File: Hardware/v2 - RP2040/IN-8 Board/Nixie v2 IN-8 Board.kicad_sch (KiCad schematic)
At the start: 31 parts, among them J1 Conn_01x10_Pin, J2 Conn_01x10_Pin, J3 Conn_01x10_Pin, Q1 MMBTA42, Q2 PZTA92, U1 NCH8200HV, U2 VEML7700, U3 К155ИД1, U4 К155ИД1, U5 К155ИД1, U6 К155ИД1

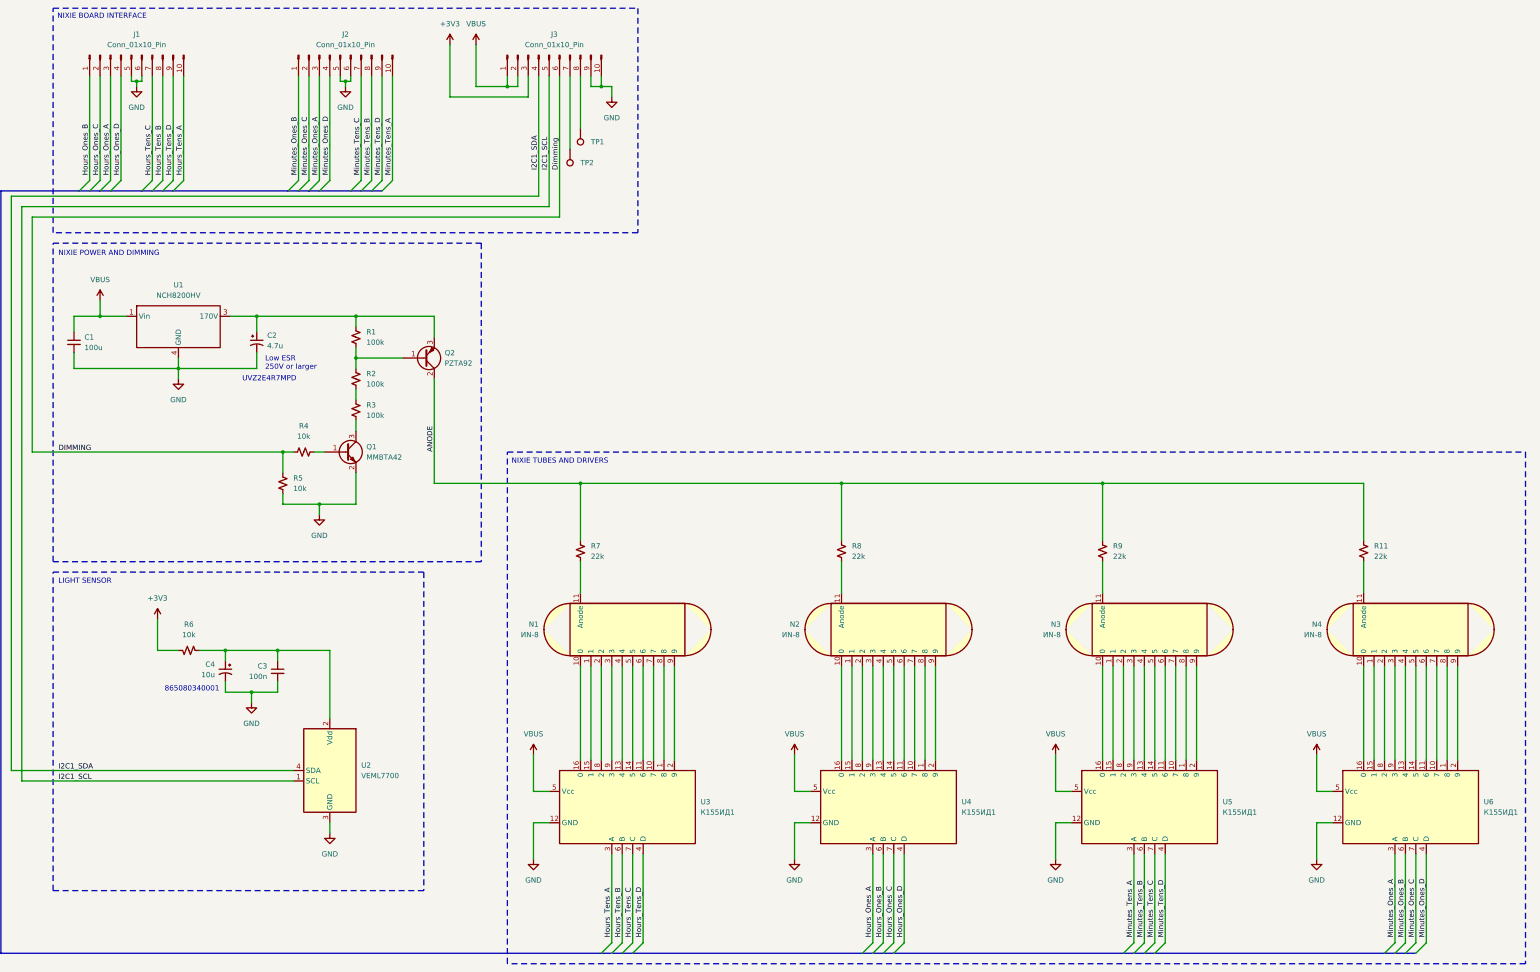
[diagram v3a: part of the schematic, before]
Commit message: started nixie layout, added bleed resistor to HV cap
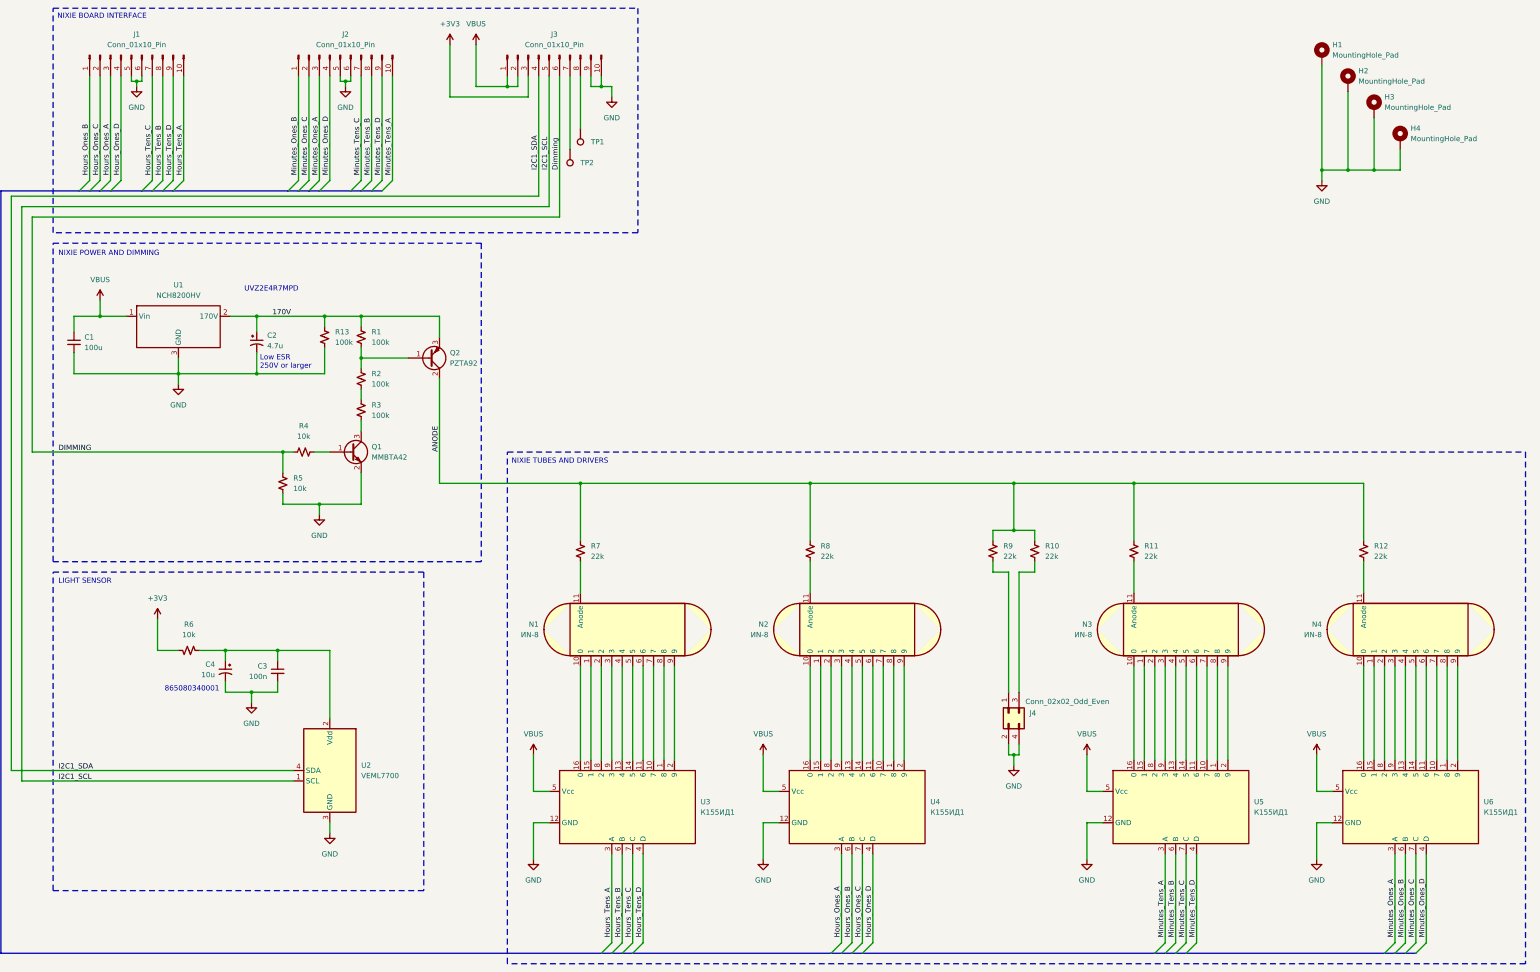
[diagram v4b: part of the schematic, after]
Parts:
- added H1, H2, H3, H4: MountingHole_Pad, MountingHole:MountingHole_3.2mm_M3_Pad_Via, symbol Mechanical:MountingHole_Pad
- added J4: Conn_02x02_Odd_Even, Connector_PinSocket_2.54mm:PinSocket_2x02_P2.54mm_Vertical, symbol Connector_Generic:Conn_02x02_Odd_Even
- added R10, R9: 22k, Resistor_SMD:R_0805_2012Metric, symbol Device:R_Small_US
- added R13: 100k, Resistor_SMD:R_0805_2012Metric, symbol Device:R_Small_US
- J1, J2, J3: footprint Connector_PinHeader_2.54mm:PinHeader_2x05_P2.54mm_Horizontal -> Connector_PinHeader_2.54mm:PinHeader_2x05_P2.54mm_Vertical
- renumbered R9 to R11, R11 to R12
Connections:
- net ANODE: now also R10.1, R9.1
- net GND: now also U1.3 (GND), H1.1, H2.1, H3.1, H4.1, J4.2 (Pin_2), J4.4 (Pin_4), R13.2; no longer U1.2 (GND)
- net 170V: now reaches C2.1, Q2.3 (E), R1.1
- net 170V: now also U1.2 (170V), R13.1; no longer U1.3 (170V)
- new net: J4.3 (Pin_3), R10.2
- new net: J4.1 (Pin_1), R9.2
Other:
- moved on the sheet: N2, N3, Q1, Q2, R1, R11, R2, R3, R8, U4, U5

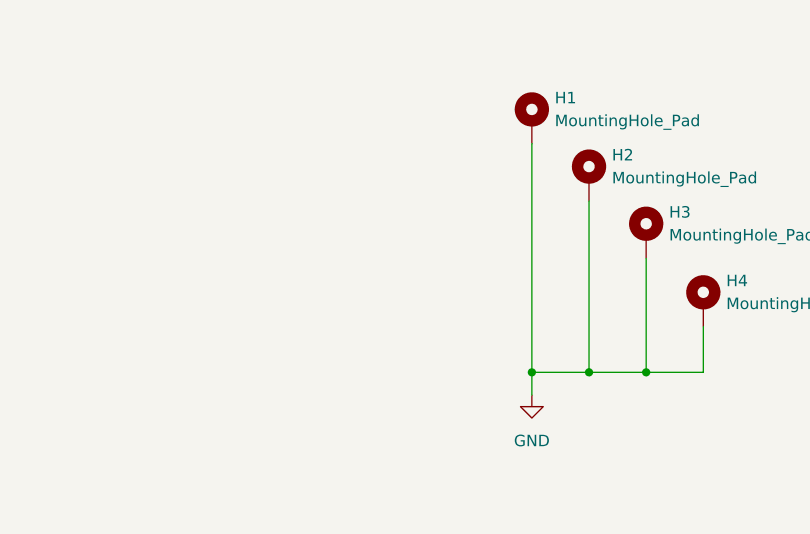
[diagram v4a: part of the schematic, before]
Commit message: finished initial layout and swapped SDA/SCL on connector
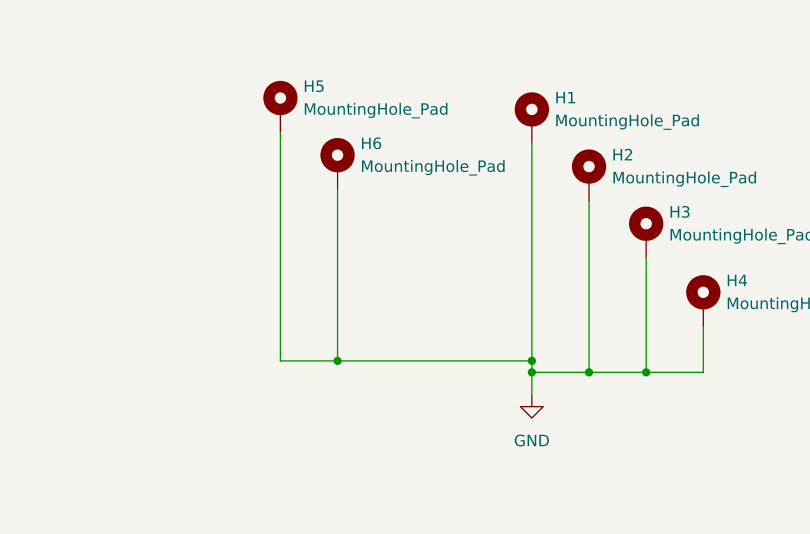
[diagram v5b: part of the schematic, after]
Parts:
- added H5, H6: MountingHole_Pad, MountingHole:MountingHole_3.2mm_M3_Pad_Via, symbol Mechanical:MountingHole_Pad
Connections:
- net GND: now also H5.1, H6.1
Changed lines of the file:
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@@
 	)
 	(junction
+		(at 332.74 54.61)
+		(diameter 0)
+		(color 0 0 0 0)
+	)
+	(junction
 		(at 173.99 132.08)
 		(diameter 0)
@@
 	)
 	(junction
+		(at 354.33 54.61)
+		(diameter 0)
+		(color 0 0 0 0)
+	)
+	(junction
 		(at 156.21 35.56)
 		(diameter 0)
@@
 		)
 	)
-	(wire
-		(pts
-			(xy 38.1 64.77) (xy 166.37 64.77)
-		)
-		(stroke
-			(width 0)
-			(type default)
-		)
-	)
 	(bus
 		(pts
@@
 	(wire
 		(pts
+			(xy 163.83 33.02) (xy 163.83 62.23)
+		)
+		(stroke
+			(width 0)
+			(type default)
+		)
+	)
+	(wire
+		(pts
 			(xy 148.59 35.56) (xy 156.21 35.56)
 		)
@@
 	(wire
 		(pts
-			(xy 163.83 33.02) (xy 163.83 62.23)
+			(xy 166.37 207.01) (xy 162.56 207.01)
 		)
 		(stroke
@@
 	(wire
 		(pts
-			(xy 166.37 207.01) (xy 162.56 207.01)
+			(xy 372.11 176.53) (xy 372.11 199.39)
 		)
 		(stroke
@@
 	(wire
 		(pts
-			(xy 372.11 176.53) (xy 372.11 199.39)
+			(xy 279.4 143.51) (xy 284.48 143.51)
 		)
 		(stroke
@@
 	(wire
 		(pts
-			(xy 279.4 143.51) (xy 284.48 143.51)
+			(xy 326.39 54.61) (xy 332.74 54.61)
 		)
 		(stroke
@@
 	(wire
 		(pts
+			(xy 332.74 54.61) (xy 354.33 54.61)
+		)
+		(stroke
+			(width 0)
+			(type default)
+		)
+	)
+	(wire
+		(pts
 			(xy 69.85 33.02) (xy 69.85 58.42)
 		)
@@
 	(wire
 		(pts
+			(xy 38.1 64.77) (xy 166.37 64.77)
+		)
+		(stroke
+			(width 0)
+			(type default)
+		)
+	)
+	(wire
+		(pts
 			(xy 54.61 33.02) (xy 54.61 58.42)
 		)
@@
 	(wire
 		(pts
+			(xy 166.37 33.02) (xy 166.37 64.77)
+		)
+		(stroke
+			(width 0)
+			(type default)
+		)
+	)
+	(wire
+		(pts
 			(xy 364.49 176.53) (xy 364.49 199.39)
 		)
@@
 	(wire
 		(pts
-			(xy 166.37 33.02) (xy 166.37 64.77)
-		)
-		(stroke
-			(width 0)
-			(type default)
-		)
-	)
-	(wire
-		(pts
 			(xy 116.84 34.29) (xy 118.11 34.29)
 		)
@@
 	(wire
 		(pts
+			(xy 332.74 35.56) (xy 332.74 54.61)
+		)
+		(stroke
+			(width 0)
+			(type default)
+		)
+	)
+	(wire
+		(pts
 			(xy 64.77 34.29) (xy 66.04 34.29)
 		)
@@
 	(wire
 		(pts
+			(xy 354.33 54.61) (xy 354.33 30.48)
+		)
+		(stroke
+			(width 0)
+			(type default)
+		)
+	)
+	(wire
+		(pts
 			(xy 173.99 132.08) (xy 173.99 146.05)
 		)
@@
 	(wire
 		(pts
-			(xy 354.33 55.88) (xy 354.33 30.48)
+			(xy 354.33 55.88) (xy 354.33 54.61)
 		)
 		(stroke
@@
 	(wire
 		(pts
+			(xy 326.39 54.61) (xy 326.39 29.21)
+		)
+		(stroke
+			(width 0)
+			(type default)
+		)
+	)
+	(wire
+		(pts
 			(xy 105.41 33.02) (xy 105.41 58.42)
 		)
@@
 		)
 	)
+	(label "I2C1_SCL"
+		(at 166.37 55.88 90)
+		(fields_autoplaced yes)
+		(effects
+			(font
+				(size 1.27 1.27)
+			)
+			(justify left bottom)
+		)
+	)
 	(label "Hours_Ones_C"
 		(at 57.15 57.15 90)
@@
 		)
 	)
+	(label "I2C1_SDA"
+		(at 163.83 55.88 90)
+		(fields_autoplaced yes)
+		(effects
+			(font
+				(size 1.27 1.27)
+			)
+			(justify left bottom)
+		)
+	)
 	(label "Minutes_Ones_D"
 		(at 113.03 57.15 90)
@@
 		)
 	)
-	(label "I2C1_SCL"
-		(at 166.37 55.88 90)
-		(fields_autoplaced yes)
-		(effects
-			(font
-				(size 1.27 1.27)
-			)
-			(justify left bottom)
-		)
-	)
 	(label "ANODE"
 		(at 139.7 118.11 270)
@@
 		)
 	)
-	(label "I2C1_SDA"
-		(at 163.83 55.88 90)
-		(fields_autoplaced yes)
-		(effects
-			(font
-				(size 1.27 1.27)
-			)
-			(justify left bottom)
-		)
-	)
 	(label "Minutes_Tens_C"
 		(at 120.65 57.15 90)
@@
 	)
 	(symbol
+		(lib_id "Mechanical:MountingHole_Pad")
+		(at 332.74 33.02 0)
+		(unit 1)
+		(exclude_from_sim yes)
+		(in_bom no)
+		(on_board yes)
+		(dnp no)
+		(fields_autoplaced yes)
+		(property "Reference" "H6"
+			(at 335.28 30.4799 0)
+			(effects
+				(font
+					(size 1.27 1.27)
+				)
+				(justify left)
+			)
+		)
+		(property "Value" "MountingHole_Pad"
+			(at 335.28 33.0199 0)
+			(effects
+				(font
+					(size 1.27 1.27)
+				)
+				(justify left)
+			)
+		)
+		(property "Footprint" "MountingHole:MountingHole_3.2mm_M3_Pad_Via"
+			(at 332.74 33.02 0)
+			(effects
+				(font
+					(size 1.27 1.27)
+				)
+				(hide yes)
+			)
+		)
+		(property "Datasheet" "~"
+			(at 332.74 33.02 0)
+			(effects
+				(font
+					(size 1.27 1.27)
+				)
+				(hide yes)
+			)
+		)
+		(property "Description" "Mounting Hole with connection"
+			(at 332.74 33.02 0)
+			(effects
+				(font
+					(size 1.27 1.27)
+				)
+				(hide yes)
+			)
+		)
+		(pin "1"
+		)
+		(instances
+			(project "Nixie v2 IN-8 Board"
+				(path "/5c74cb95-ab53-4089-bee1-f337a16e1c0e"
+					(reference "H6")
+					(unit 1)
+				)
+			)
+		)
+	)
+	(symbol
 		(lib_id "Device:C_Polarized_Small_US")
 		(at 87.63 177.8 0)
@@
 					(unit 1)
 				)
+			)
+		)
+	)
+	(symbol
+		(lib_id "Mechanical:MountingHole_Pad")
+		(at 326.39 26.67 0)
+		(unit 1)
+		(exclude_from_sim yes)
+		(in_bom no)
+		(on_board yes)
+		(dnp no)
+		(fields_autoplaced yes)
+		(property "Reference" "H5"
+			(at 328.93 24.1299 0)
+			(effects
+				(font
+					(size 1.27 1.27)
+				)
+				(justify left)
+			)
+		)
+		(property "Value" "MountingHole_Pad"
+			(at 328.93 26.6699 0)
+			(effects
+				(font
+					(size 1.27 1.27)
+				)
+				(justify left)
+			)
+		)
+		(property "Footprint" "MountingHole:MountingHole_3.2mm_M3_Pad_Via"
+			(at 326.39 26.67 0)
+			(effects
+				(font
+					(size 1.27 1.27)
+				)
+				(hide yes)
+			)
+		)
+		(property "Datasheet" "~"
+			(at 326.39 26.67 0)
+			(effects
+				(font
+					(size 1.27 1.27)
+				)
+				(hide yes)
+			)
+		)
+		(property "Description" "Mounting Hole with connection"
+			(at 326.39 26.67 0)
+			(effects
+				(font
+					(size 1.27 1.27)
+				)
+				(hide yes)
+			)
+		)
+		(pin "1"
+		)
+		(instances
+			(project "Nixie v2 IN-8 Board"
+				(path "/5c74cb95-ab53-4089-bee1-f337a16e1c0e"
+					(reference "H5")
+					(unit 1)
+				)
